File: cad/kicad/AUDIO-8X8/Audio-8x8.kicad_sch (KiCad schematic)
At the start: 21 parts, among them J101 AUDIO_TDM_CONTROL, J102 AUDIO_12V_POWER, J201 NC3MAV, J202 NC3MAV, J203 NC3MAV, J204 NC3MAV, J205 NC3MAV, J206 NC3MAV, J207 NC3MAV, J208 NC3MAV, J301 NC3FAV, J302 NC3FAV, J303 NC3FAV, J304 NC3FAV, J305 NC3FAV, J306 NC3FAV, J307 NC3FAV, J308 NC3FAV, J901 CHASSIS_BOND_TEST

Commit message: Add controlled connector footprint audit
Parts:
- J201, J202, J203, J204, J205, J206, J207, J208: footprint (none) -> Connector_Audio:Jack_XLR_Neutrik_NC3MAV_Vertical
- J301, J302, J303, J304, J305, J306, J307, J308: footprint (none) -> Connector_Audio:Jack_XLR_Neutrik_NC3FAV_Vertical
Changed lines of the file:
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@@
+			)
+		)
+		(property "Footprint" "Connector_Audio:Jack_XLR_Neutrik_NC3MAV_Vertical"
+			(at 54.61 46.99 0.0000)
+			(effects
+				(font
+					(size 1.27 1.27)
+				)
+				(hide yes)
 			)
 		)
@@
 			)
 		)
+		(property "Footprint" "Connector_Audio:Jack_XLR_Neutrik_NC3FAV_Vertical"
+			(at 149.86 46.99 0.0000)
+			(effects
+				(font
+					(size 1.27 1.27)
+				)
+				(hide yes)
+			)
+		)
 		(property "Manufacturer" "Neutrik"
 			(at 152.4 52.0699 0)
@@
 			)
 		)
+		(property "Footprint" "Connector_Audio:Jack_XLR_Neutrik_NC3MAV_Vertical"
+			(at 54.61 86.36 0.0000)
+			(effects
+				(font
+					(size 1.27 1.27)
+				)
+				(hide yes)
+			)
+		)
 		(property "Manufacturer" "Neutrik"
 			(at 57.15 91.4399 0)
@@
 			)
 		)
+		(property "Footprint" "Connector_Audio:Jack_XLR_Neutrik_NC3FAV_Vertical"
+			(at 149.86 86.36 0.0000)
+			(effects
+				(font
+					(size 1.27 1.27)
+				)
+				(hide yes)
+			)
+		)
 		(property "Manufacturer" "Neutrik"
 			(at 152.4 91.4399 0)
@@
 			)
 		)
+		(property "Footprint" "Connector_Audio:Jack_XLR_Neutrik_NC3MAV_Vertical"
+			(at 54.61 124.46 0.0000)
+			(effects
+				(font
+					(size 1.27 1.27)
+				)
+				(hide yes)
+			)
+		)
 		(property "Manufacturer" "Neutrik"
 			(at 57.15 129.5399 0)
@@
 			)
 		)
+		(property "Footprint" "Connector_Audio:Jack_XLR_Neutrik_NC3FAV_Vertical"
+			(at 149.86 124.46 0.0000)
+			(effects
+				(font
+					(size 1.27 1.27)
+				)
+				(hide yes)
+			)
+		)
 		(property "Manufacturer" "Neutrik"
 			(at 152.4 129.5399 0)
@@
 			)
 		)
+		(property "Footprint" "Connector_Audio:Jack_XLR_Neutrik_NC3MAV_Vertical"
+			(at 54.61 163.83 0.0000)
+			(effects
+				(font
+					(size 1.27 1.27)
+				)
+				(hide yes)
+			)
+		)
 		(property "Manufacturer" "Neutrik"
 			(at 57.15 168.9099 0)
@@
 			)
 		)
+		(property "Footprint" "Connector_Audio:Jack_XLR_Neutrik_NC3FAV_Vertical"
+			(at 149.86 163.83 0.0000)
+			(effects
+				(font
+					(size 1.27 1.27)
+				)
+				(hide yes)
+			)
+		)
 		(property "Manufacturer" "Neutrik"
 			(at 152.4 168.9099 0)
@@
 			)
 		)
+		(property "Footprint" "Connector_Audio:Jack_XLR_Neutrik_NC3MAV_Vertical"
+			(at 54.61 203.2 0.0000)
+			(effects
+				(font
+					(size 1.27 1.27)
+				)
+				(hide yes)
+			)
+		)
 		(property "Manufacturer" "Neutrik"
 			(at 57.15 208.2799 0)
@@
 			)
 		)
+		(property "Footprint" "Connector_Audio:Jack_XLR_Neutrik_NC3FAV_Vertical"
+			(at 149.86 203.2 0.0000)
+			(effects
+				(font
+					(size 1.27 1.27)
+				)
+				(hide yes)
+			)
+		)
 		(property "Manufacturer" "Neutrik"
 			(at 152.4 208.2799 0)
@@
 			)
 		)
+		(property "Footprint" "Connector_Audio:Jack_XLR_Neutrik_NC3MAV_Vertical"
+			(at 54.61 242.57 0.0000)
+			(effects
+				(font
+					(size 1.27 1.27)
+				)
+				(hide yes)
+			)
+		)
 		(property "Manufacturer" "Neutrik"
 			(at 57.15 247.6499 0)
@@
 			)
 		)
+		(property "Footprint" "Connector_Audio:Jack_XLR_Neutrik_NC3FAV_Vertical"
+			(at 149.86 242.57 0.0000)
+			(effects
+				(font
+					(size 1.27 1.27)
+				)
+				(hide yes)
+			)
+		)
 		(property "Manufacturer" "Neutrik"
 			(at 152.4 247.6499 0)
@@
 			)
 		)
+		(property "Footprint" "Connector_Audio:Jack_XLR_Neutrik_NC3MAV_Vertical"
+			(at 54.61 280.67 0.0000)
+			(effects
+				(font
+					(size 1.27 1.27)
+				)
+				(hide yes)
+			)
+		)
 		(property "Manufacturer" "Neutrik"
 			(at 57.15 285.7499 0)
@@
 			)
 		)
+		(property "Footprint" "Connector_Audio:Jack_XLR_Neutrik_NC3FAV_Vertical"
+			(at 149.86 280.67 0.0000)
+			(effects
+				(font
+					(size 1.27 1.27)
+				)
+				(hide yes)
+			)
+		)
 		(property "Manufacturer" "Neutrik"
 			(at 152.4 285.7499 0)
@@
 			)
 		)
+		(property "Footprint" "Connector_Audio:Jack_XLR_Neutrik_NC3MAV_Vertical"
+			(at 54.61 320.04 0.0000)
+			(effects
+				(font
+					(size 1.27 1.27)
+				)
+				(hide yes)
+			)
+		)
 		(property "Manufacturer" "Neutrik"
 			(at 57.15 325.1199 0)
@@
 				(hide yes)
 			)
+		)
+		(property "Footprint" "Connector_Audio:Jack_XLR_Neutrik_NC3FAV_Vertical"
+			(at 149.86 320.04 0.0000)
+			(effects
+				(font
+					(size 1.27 1.27)
+				)
+				(hide yes)
+			)

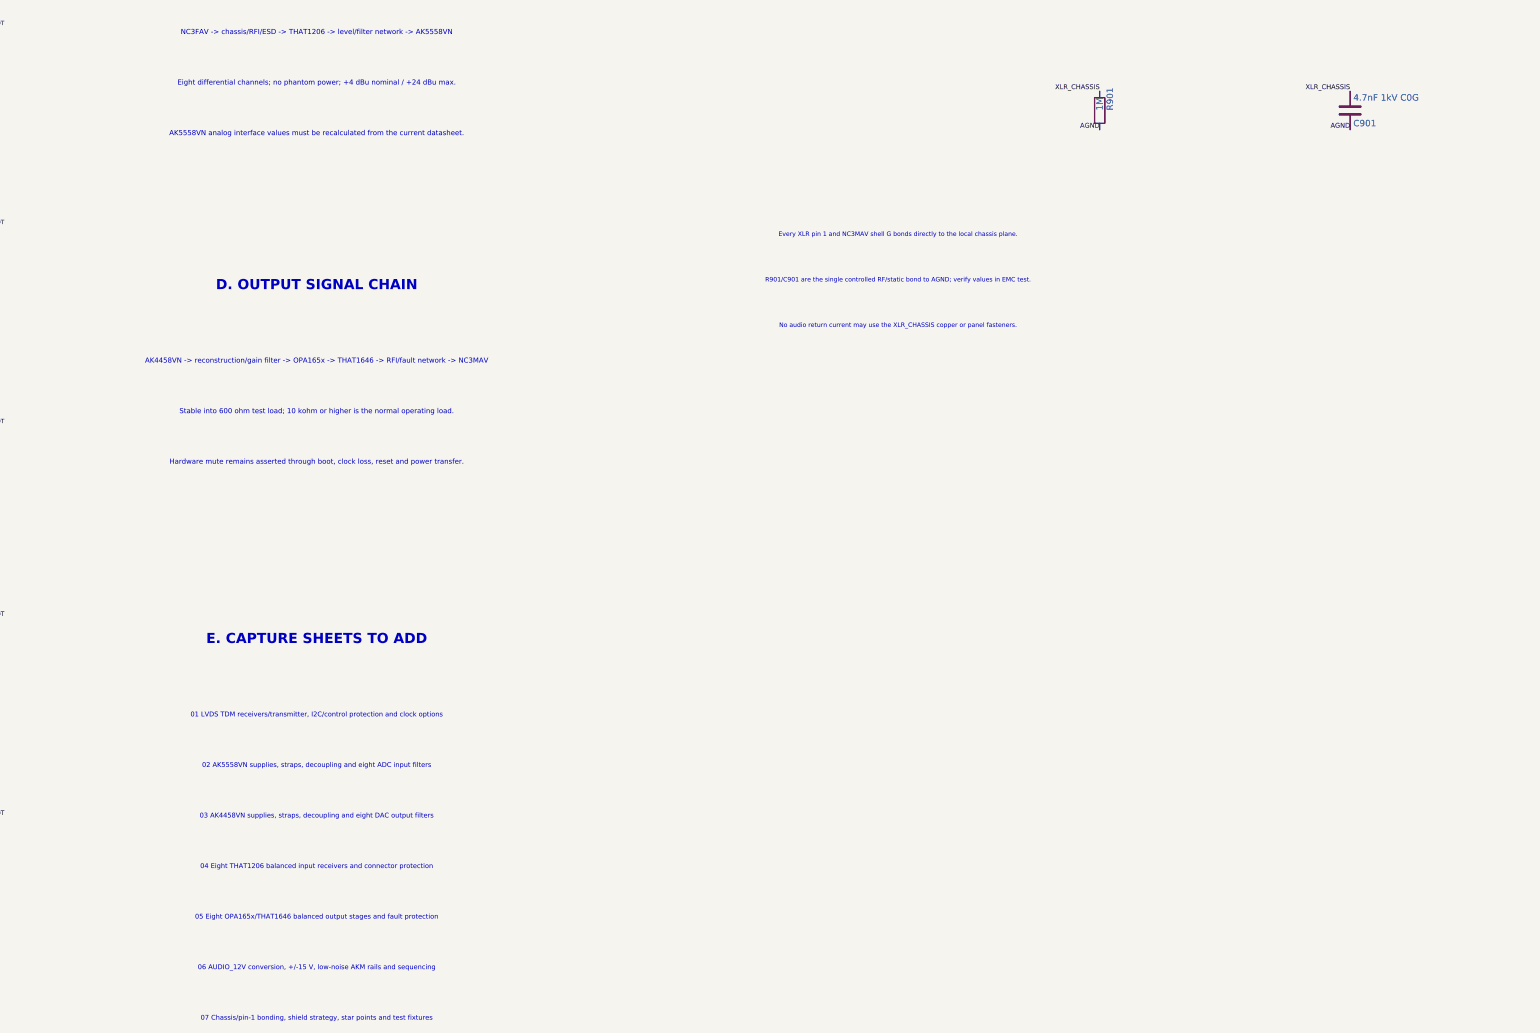
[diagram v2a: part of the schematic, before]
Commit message: Complete A1 detailed carrier and audio capture
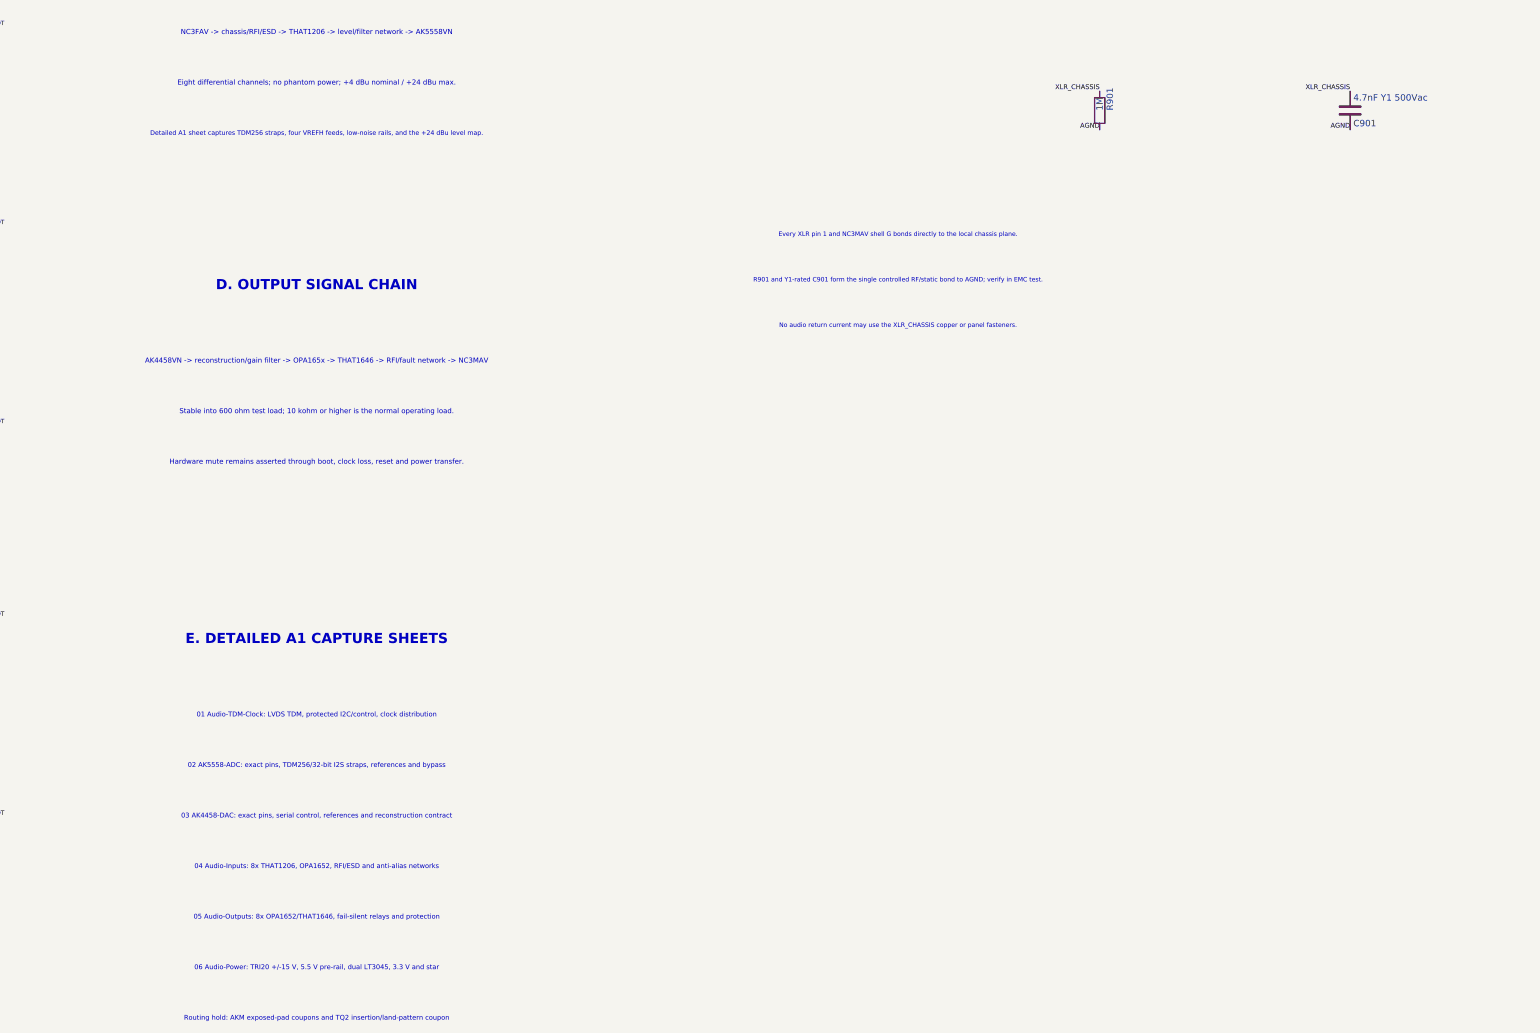
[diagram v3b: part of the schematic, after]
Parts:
- C901: value 4.7nF 1kV C0G -> 4.7nF Y1 500Vac; footprint (none) -> Capacitor_THT:C_Disc_D16.0mm_W5.0mm_P10.00mm; MPN (none) -> VY1472M63Y5UQ6TV0; Manufacturer (none) -> Vishay
- J101: footprint (none) -> Connector_Molex_Milligrid:Molex_8783230xx_2x15_P2.0mm_Header_Vertical_Polarized_MountingPegs; MPN (none) -> 87832-6423; Manufacturer (none) -> Molex
- J901: footprint (none) -> TestPoint:TestPoint_2Pads_Pitch2.54mm_Drill0.8mm
- R901: footprint (none) -> Resistor_SMD:R_0603_1608Metric; MPN (none) -> RC0603FR-071ML; Manufacturer (none) -> Yageo
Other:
- note added: "01 Audio-TDM-Clock: LVDS TDM, protected I2C/control, clock distribution"
- note added: "02 AK5558-ADC: exact pins, TDM256/32-bit I2S straps, references and bypass"
- note added: "03 AK4458-DAC: exact pins, serial control, references and reconstruction contract"
- note added: "04 Audio-Inputs: 8x THAT1206, OPA1652, RFI/ESD and anti-alias networks"
- note added: "05 Audio-Outputs: 8x OPA1652/THAT1646, fail-silent relays and protection"
- note added: "06 Audio-Power: TRI20 +/-15 V, 5.5 V pre-rail, dual LT3045, 3.3 V and star"
- note added: "Detailed A1 sheet captures TDM256 straps, four VREFH feeds, low-noise rails, and the +24 dBu level map."
- note added: "E. DETAILED A1 CAPTURE SHEETS"
- note added: "R901 and Y1-rated C901 form the single controlled RF/static bond to AGND; verify in EMC test."
- note added: "Routing hold: AKM exposed-pad coupons and TQ2 insertion/land-pattern coupon"
- note removed: "01 LVDS TDM receivers/transmitter, I2C/control protection and clock options"
- note removed: "02 AK5558VN supplies, straps, decoupling and eight ADC input filters"
- note removed: "03 AK4458VN supplies, straps, decoupling and eight DAC output filters"
- note removed: "04 Eight THAT1206 balanced input receivers and connector protection"
- note removed: "05 Eight OPA165x/THAT1646 balanced output stages and fault protection"
- note removed: "06 AUDIO_12V conversion, +/-15 V, low-noise AKM rails and sequencing"
- note removed: "07 Chassis/pin-1 bonding, shield strategy, star points and test fixtures"
- note removed: "AK5558VN analog interface values must be recalculated from the current datasheet."
- note removed: "E. CAPTURE SHEETS TO ADD"
- note removed: "R901/C901 are the single controlled RF/static bond to AGND; verify values in EMC test."
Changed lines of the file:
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@@
 	(title_block
 		(title "Radxa CM5 ProComm Audio 8x8 - Interface Contract")
-		(date "2026-08-13")
-		(rev "A0")
+		(date "2026-08-16")
+		(rev "A1")
 		(company "ProComm")
 		(comment 1 "AK5558VN ADC and AK4458VN DAC over buffered differential TDM")
 		(comment 2 "+4 dBu nominal, +24 dBu maximum, active-balanced XLR stages")
 		(comment 3 "Left bank male outputs; right bank female inputs")
-		(comment 4 "NOT A FABRICATION RELEASE - AKM networks require datasheet calculation")
+		(comment 4 "ENGINEERING CAPTURE - detailed sheets complete; coupon and bench gates remain")
 	)
 	(symbol
@@
 		(instances
 			(project "Audio-8x8"
-				(path "/bc22b7a4-5d66-56d7-9333-8e9e18df35f1"
+				(path "/72a0207f-1b95-5f12-8fde-6fa66f7cdabb"
 					(reference "J201")
 					(unit 1)
@@
 		(instances
 			(project "Audio-8x8"
-				(path "/bc22b7a4-5d66-56d7-9333-8e9e18df35f1"
+				(path "/72a0207f-1b95-5f12-8fde-6fa66f7cdabb"
 					(reference "J301")
 					(unit 1)
@@
 		(instances
 			(project "Audio-8x8"
-				(path "/bc22b7a4-5d66-56d7-9333-8e9e18df35f1"
+				(path "/72a0207f-1b95-5f12-8fde-6fa66f7cdabb"
 					(reference "J202")
 					(unit 1)
@@
 		(instances
 			(project "Audio-8x8"
-				(path "/bc22b7a4-5d66-56d7-9333-8e9e18df35f1"
+				(path "/72a0207f-1b95-5f12-8fde-6fa66f7cdabb"
 					(reference "J302")
 					(unit 1)
@@
 		(instances
 			(project "Audio-8x8"
-				(path "/bc22b7a4-5d66-56d7-9333-8e9e18df35f1"
+				(path "/72a0207f-1b95-5f12-8fde-6fa66f7cdabb"
 					(reference "J203")
 					(unit 1)
@@
 		(instances
 			(project "Audio-8x8"
-				(path "/bc22b7a4-5d66-56d7-9333-8e9e18df35f1"
+				(path "/72a0207f-1b95-5f12-8fde-6fa66f7cdabb"
 					(reference "J303")
 					(unit 1)
@@
 		(instances
 			(project "Audio-8x8"
-				(path "/bc22b7a4-5d66-56d7-9333-8e9e18df35f1"
+				(path "/72a0207f-1b95-5f12-8fde-6fa66f7cdabb"
 					(reference "J204")
 					(unit 1)
@@
 		(instances
 			(project "Audio-8x8"
-				(path "/bc22b7a4-5d66-56d7-9333-8e9e18df35f1"
+				(path "/72a0207f-1b95-5f12-8fde-6fa66f7cdabb"
 					(reference "J304")
 					(unit 1)
@@
 		(instances
 			(project "Audio-8x8"
-				(path "/bc22b7a4-5d66-56d7-9333-8e9e18df35f1"
+				(path "/72a0207f-1b95-5f12-8fde-6fa66f7cdabb"
 					(reference "J205")
 					(unit 1)
@@
 		(instances
 			(project "Audio-8x8"
-				(path "/bc22b7a4-5d66-56d7-9333-8e9e18df35f1"
+				(path "/72a0207f-1b95-5f12-8fde-6fa66f7cdabb"
 					(reference "J305")
 					(unit 1)
@@
 		(instances
 			(project "Audio-8x8"
-				(path "/bc22b7a4-5d66-56d7-9333-8e9e18df35f1"
+				(path "/72a0207f-1b95-5f12-8fde-6fa66f7cdabb"
 					(reference "J206")
 					(unit 1)
@@
 		(instances
 			(project "Audio-8x8"
-				(path "/bc22b7a4-5d66-56d7-9333-8e9e18df35f1"
+				(path "/72a0207f-1b95-5f12-8fde-6fa66f7cdabb"
 					(reference "J306")
 					(unit 1)
@@
 		(instances
 			(project "Audio-8x8"
-				(path "/bc22b7a4-5d66-56d7-9333-8e9e18df35f1"
+				(path "/72a0207f-1b95-5f12-8fde-6fa66f7cdabb"
 					(reference "J207")
 					(unit 1)
@@
 		(instances
 			(project "Audio-8x8"
-				(path "/bc22b7a4-5d66-56d7-9333-8e9e18df35f1"
+				(path "/72a0207f-1b95-5f12-8fde-6fa66f7cdabb"
 					(reference "J307")
 					(unit 1)
@@
 		(instances
 			(project "Audio-8x8"
-				(path "/bc22b7a4-5d66-56d7-9333-8e9e18df35f1"
+				(path "/72a0207f-1b95-5f12-8fde-6fa66f7cdabb"
 					(reference "J208")
 					(unit 1)
@@
 		(instances
 			(project "Audio-8x8"
-				(path "/bc22b7a4-5d66-56d7-9333-8e9e18df35f1"
+				(path "/72a0207f-1b95-5f12-8fde-6fa66f7cdabb"
 					(reference "J308")
 					(unit 1)
@@
 			)
 		)
+		(property "Footprint" "Connector_Molex_Milligrid:Molex_8783230xx_2x15_P2.0mm_Header_Vertical_Polarized_MountingPegs"
+			(at 284.48 72.39 0.0000)
+			(effects
+				(font
+					(size 1.27 1.27)
+				)
+				(hide yes)
+			)
+		)
+		(property "Manufacturer" "Molex"
+			(at 287.02 77.4699 0)
+			(effects
+				(font
+					(size 1.27 1.27)
+				)
+				(hide yes)
+			)
+		)
+		(property "MPN" "87832-6423"
+			(at 287.02 77.4699 0)
+			(effects
+				(font
+					(size 1.27 1.27)
+				)
+				(hide yes)
+			)
+		)
 		(pin "1"
 		)
@@
 		(instances
 			(project "Audio-8x8"
-				(path "/bc22b7a4-5d66-56d7-9333-8e9e18df35f1"
+				(path "/72a0207f-1b95-5f12-8fde-6fa66f7cdabb"
 					(reference "J101")
 					(unit 1)
@@
 		(instances
 			(project "Audio-8x8"
-				(path "/bc22b7a4-5d66-56d7-9333-8e9e18df35f1"
+				(path "/72a0207f-1b95-5f12-8fde-6fa66f7cdabb"
 					(reference "J102")
 					(unit 1)
@@
 			)
 		)
+		(property "Footprint" "Resistor_SMD:R_0603_1608Metric"
+			(at 388.112 180.34 90)
+			(effects
+				(font
+					(size 1.27 1.27)
+				)
+				(hide yes)
+			)
+		)
+		(property "Manufacturer" "Yageo"
+			(at 392.43 185.4199 0)
+			(effects
+				(font
+					(size 1.27 1.27)
+				)
+				(hide yes)
+			)
+		)
+		(property "MPN" "RC0603FR-071ML"
+			(at 392.43 185.4199 0)
+			(effects
+				(font
+					(size 1.27 1.27)
+				)
+				(hide yes)
+			)
+		)
 		(pin "1"
 		)
@@
 		(instances
 			(project "Audio-8x8"
-				(path "/bc22b7a4-5d66-56d7-9333-8e9e18df35f1"
+				(path "/72a0207f-1b95-5f12-8fde-6fa66f7cdabb"
 					(reference "R901")
 					(unit 1)
@@
 			)
 		)
-		(property "Value" "4.7nF 1kV C0G"
+		(property "Value" "4.7nF Y1 500Vac"
 			(at 440.055 177.8 0.0000)
 			(effects
@@
 			)
 		)
+		(property "Footprint" "Capacitor_THT:C_Disc_D16.0mm_W5.0mm_P10.00mm"
+			(at 440.3852 176.53 0.0000)
+			(effects
+				(font
+					(size 1.27 1.27)
+				)
+				(hide yes)
+			)
+		)
+		(property "Manufacturer" "Vishay"
+			(at 441.96 185.4199 0)
+			(effects
+				(font
+					(size 1.27 1.27)
+				)
+				(hide yes)
+			)
+		)
+		(property "MPN" "VY1472M63Y5UQ6TV0"
+			(at 441.96 185.4199 0)
+			(effects
+				(font
+					(size 1.27 1.27)
+				)
+				(hide yes)
+			)
+		)
 		(pin "1"
 		)
@@
 		(instances
 			(project "Audio-8x8"
-				(path "/bc22b7a4-5d66-56d7-9333-8e9e18df35f1"
+				(path "/72a0207f-1b95-5f12-8fde-6fa66f7cdabb"
 					(reference "C901")
 					(unit 1)
@@
 			)
 		)
+		(property "Footprint" "TestPoint:TestPoint_2Pads_Pitch2.54mm_Drill0.8mm"
+			(at 500.38 180.34 0.0000)
+			(effects
+				(font
+					(size 1.27 1.27)
+				)
+				(hide yes)
+			)
+		)
 		(pin "1"
 		)
@@
 		(instances
 			(project "Audio-8x8"
-				(path "/bc22b7a4-5d66-56d7-9333-8e9e18df35f1"
+				(path "/72a0207f-1b95-5f12-8fde-6fa66f7cdabb"
 					(reference "J901")
 					(unit 1)
@@
 		)
 	)
-	(text "AK5558VN analog interface values must be recalculated from the current datasheet."
+	(text "Detailed A1 sheet captures TDM256 straps, four VREFH feeds, low-noise rails, and the +24 dBu level map."
 		(exclude_from_sim no)
 		(at 235 185 0.0000)
 		(effects
 			(font
-				(size 1 1)
+				(size 0.9 0.9)
 			)
 		)
@@
 		)
 	)
-	(text "E. CAPTURE SHEETS TO ADD"
+	(text "E. DETAILED A1 CAPTURE SHEETS"
 		(exclude_from_sim no)
 		(at 235 285 0.0000)
@@
 		)
 	)
-	(text "01 LVDS TDM receivers/transmitter, I2C/control protection and clock options"
+	(text "01 Audio-TDM-Clock: LVDS TDM, protected I2C/control, clock distribution"
 		(exclude_from_sim no)
 		(at 235 300 0.0000)
@@
 		)
 	)
-	(text "02 AK5558VN supplies, straps, decoupling and eight ADC input filters"
+	(text "02 AK5558-ADC: exact pins, TDM256/32-bit I2S straps, references and bypass"
 		(exclude_from_sim no)
 		(at 235 310 0.0000)
@@
 		)
 	)
-	(text "03 AK4458VN supplies, straps, decoupling and eight DAC output filters"
+	(text "03 AK4458-DAC: exact pins, serial control, references and reconstruction contract"
 		(exclude_from_sim no)
 		(at 235 320 0.0000)
@@
 		)
 	)
-	(text "04 Eight THAT1206 balanced input receivers and connector protection"
+	(text "04 Audio-Inputs: 8x THAT1206, OPA1652, RFI/ESD and anti-alias networks"
 		(exclude_from_sim no)
 		(at 235 330 0.0000)
@@
 		)
 	)
-	(text "05 Eight OPA165x/THAT1646 balanced output stages and fault protection"
+	(text "05 Audio-Outputs: 8x OPA1652/THAT1646, fail-silent relays and protection"
 		(exclude_from_sim no)
 		(at 235 340 0.0000)
@@
 		)
 	)
-	(text "06 AUDIO_12V conversion, +/-15 V, low-noise AKM rails and sequencing"
+	(text "06 Audio-Power: TRI20 +/-15 V, 5.5 V pre-rail, dual LT3045, 3.3 V and star"
 		(exclude_from_sim no)
 		(at 235 350 0.0000)
@@
 		)
 	)
-	(text "07 Chassis/pin-1 bonding, shield strategy, star points and test fixtures"
+	(text "Routing hold: AKM exposed-pad coupons and TQ2 insertion/land-pattern coupon"
 		(exclude_from_sim no)
 		(at 235 360 0.0000)
@@
 		)
 	)
-	(text "R901/C901 are the single controlled RF/static bond to AGND; verify values in EMC test."
+	(text "R901 and Y1-rated C901 form the single controlled RF/static bond to AGND; verify in EMC test."
 		(exclude_from_sim no)
 		(at 350 214 0.0000)
